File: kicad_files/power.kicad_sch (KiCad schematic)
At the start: 20 parts, among them Q1 FS8205A, U1 BQ27441DRZR-G1A, U2 DW01A, U3 TPS61023DRLR

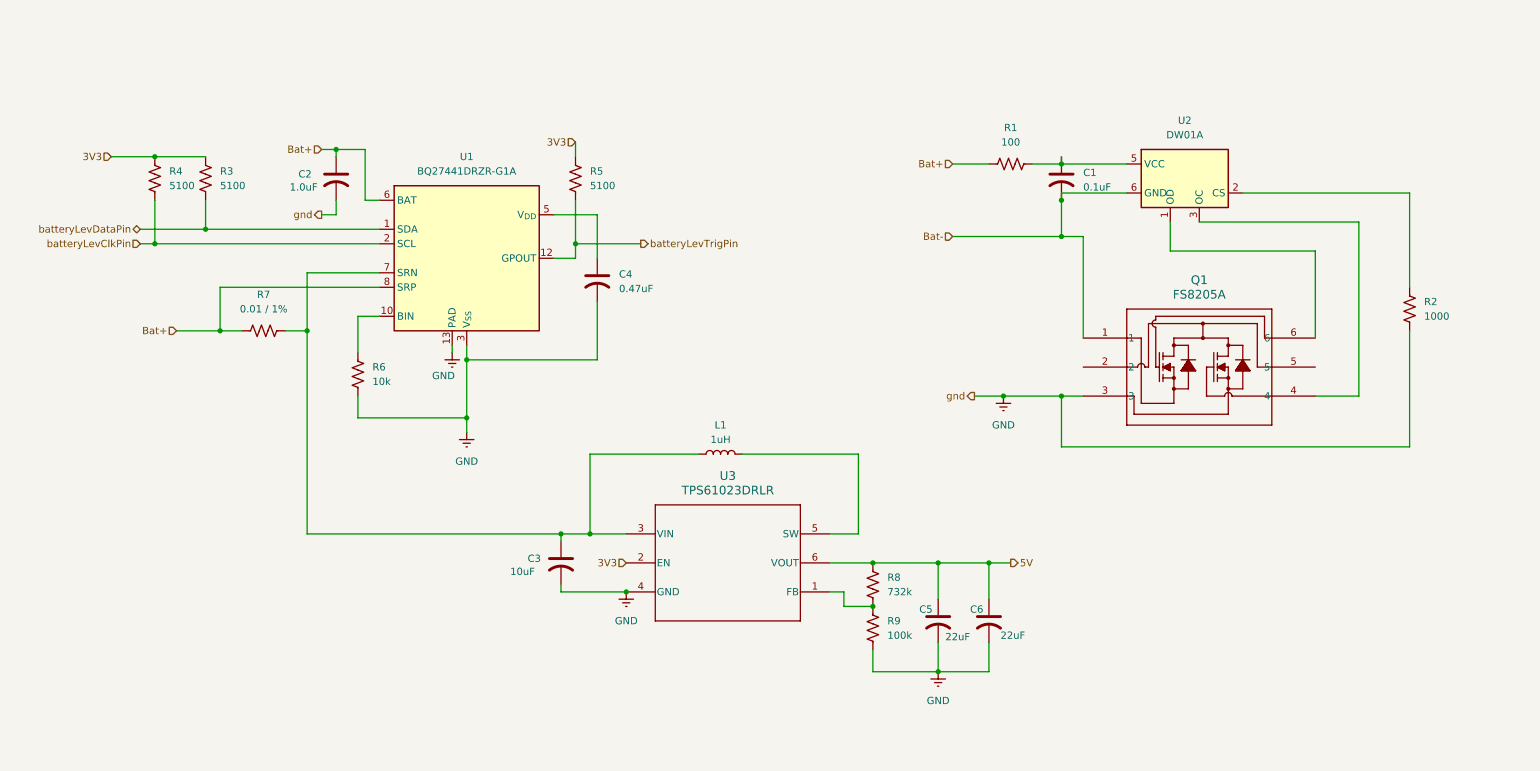
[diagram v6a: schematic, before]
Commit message: ERC errors cleaned. Hierarchical wiring finished. PWM converter change. Motor driver change.
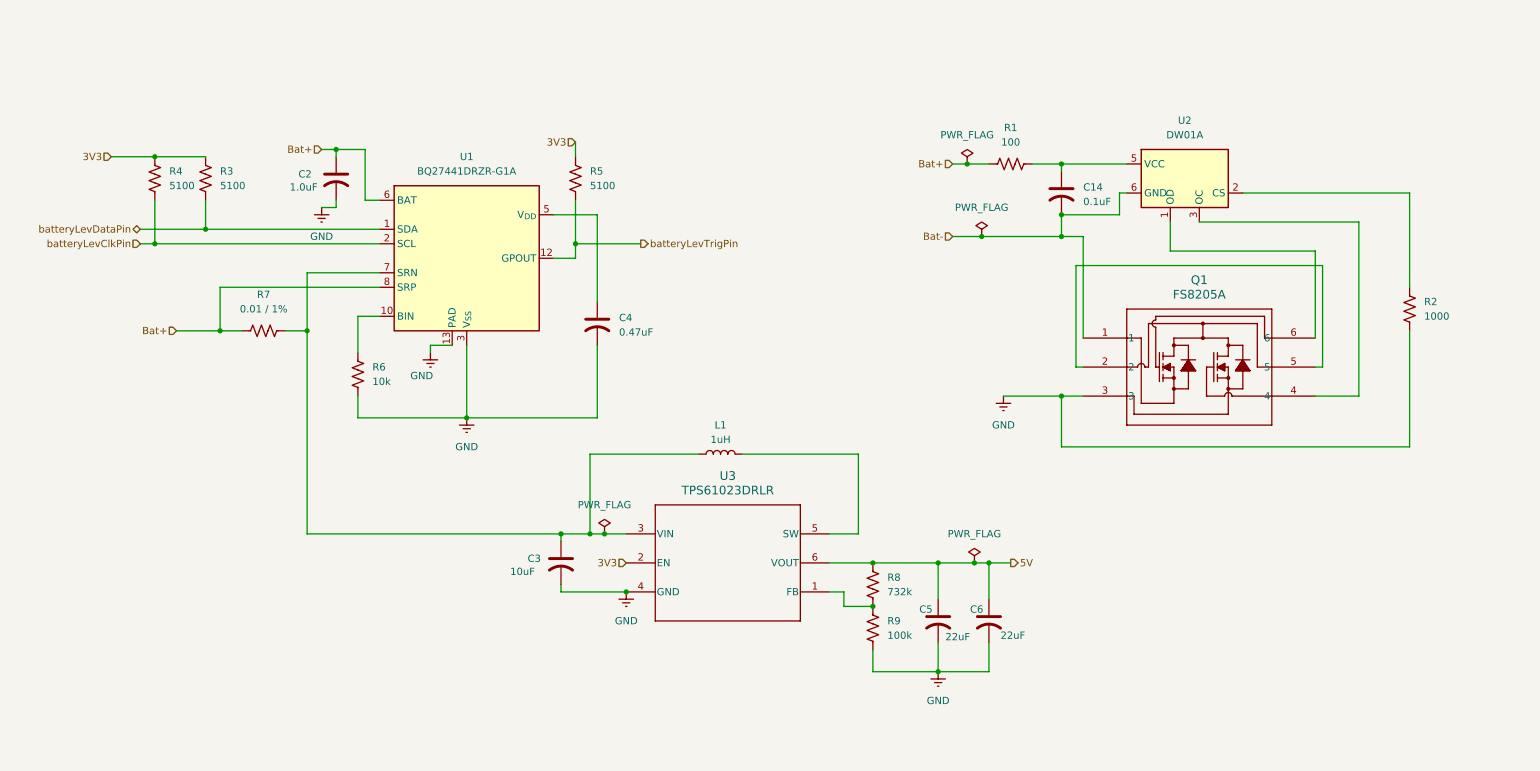
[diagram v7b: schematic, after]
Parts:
- removed C1: 0.1uF, symbol Device:C_US
- added C14: 0.1uF, symbol Device:C_US
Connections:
- net Bat-: now also C14.2
- net at R1.1, U2.5 (VCC): now also C14.1
- net at Q1.2: now also Q1.5
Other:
- moved on the sheet: C4

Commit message: Footprint assignment finished
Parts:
- C14, C2, C3, C4: footprint (none) -> Capacitor_SMD:C_1206_3216Metric_Pad1.33x1.80mm_HandSolder
- C5, C6: footprint (none) -> Capacitor_THT:CP_Radial_D5.0mm_P2.00mm
- L1: footprint (none) -> Inductor_SMD:L_1008_2520Metric_Pad1.43x2.20mm_HandSolder
- R1, R2, R3, R4, R5, R6, R7, R8, R9: footprint (none) -> Resistor_SMD:R_1206_3216Metric_Pad1.30x1.75mm_HandSolder
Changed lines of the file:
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@@
 			)
 		)
-		(property "Footprint" ""
+		(property "Footprint" "Capacitor_SMD:C_1206_3216Metric_Pad1.33x1.80mm_HandSolder"
 			(at 193.04 50.8 0)
 			(effects
@@
 			)
 		)
-		(property "Footprint" ""
+		(property "Footprint" "Resistor_SMD:R_1206_3216Metric_Pad1.30x1.75mm_HandSolder"
 			(at 161.036 119.634 90)
 			(effects
@@
 			)
 		)
-		(property "Footprint" ""
+		(property "Footprint" "Resistor_SMD:R_1206_3216Metric_Pad1.30x1.75mm_HandSolder"
 			(at 183.896 46.736 90)
 			(effects
@@
 			)
 		)
-		(property "Footprint" ""
+		(property "Footprint" "Resistor_SMD:R_1206_3216Metric_Pad1.30x1.75mm_HandSolder"
 			(at 44.196 48.514 90)
 			(effects
@@
 			)
 		)
-		(property "Footprint" ""
+		(property "Footprint" "Resistor_SMD:R_1206_3216Metric_Pad1.30x1.75mm_HandSolder"
 			(at 255.016 71.374 90)
 			(effects
@@
 			)
 		)
-		(property "Footprint" ""
+		(property "Footprint" "Capacitor_SMD:C_1206_3216Metric_Pad1.33x1.80mm_HandSolder"
 			(at 111.76 73.66 0)
 			(effects
@@
 			)
 		)
-		(property "Footprint" ""
+		(property "Footprint" "Capacitor_THT:CP_Radial_D5.0mm_P2.00mm"
 			(at 180.34 125.73 0)
 			(effects
@@
 			)
 		)
-		(property "Footprint" ""
+		(property "Footprint" "Capacitor_SMD:C_1206_3216Metric_Pad1.33x1.80mm_HandSolder"
 			(at 66.04 48.26 0)
 			(effects
@@
 			)
 		)
-		(property "Footprint" ""
+		(property "Footprint" "Inductor_SMD:L_1008_2520Metric_Pad1.43x2.20mm_HandSolder"
 			(at 133.35 96.52 0)
 			(effects
@@
 			)
 		)
-		(property "Footprint" ""
+		(property "Footprint" "Resistor_SMD:R_1206_3216Metric_Pad1.30x1.75mm_HandSolder"
 			(at 53.086 75.946 90)
 			(effects
@@
 			)
 		)
-		(property "Footprint" ""
+		(property "Footprint" "Capacitor_THT:CP_Radial_D5.0mm_P2.00mm"
 			(at 171.45 125.73 0)
 			(effects
@@
 			)
 		)
-		(property "Footprint" ""
+		(property "Footprint" "Capacitor_SMD:C_1206_3216Metric_Pad1.33x1.80mm_HandSolder"
 			(at 105.41 115.57 0)
 			(effects
@@
 			)
 		)
-		(property "Footprint" ""
+		(property "Footprint" "Resistor_SMD:R_1206_3216Metric_Pad1.30x1.75mm_HandSolder"
 			(at 161.036 127.254 90)
 			(effects
@@
 			)
 		)
-		(property "Footprint" ""
+		(property "Footprint" "Resistor_SMD:R_1206_3216Metric_Pad1.30x1.75mm_HandSolder"
 			(at 108.966 48.514 90)
 			(effects
@@
 			)
 		)
-		(property "Footprint" ""
+		(property "Footprint" "Resistor_SMD:R_1206_3216Metric_Pad1.30x1.75mm_HandSolder"
 			(at 35.306 48.514 90)
 			(effects
@@
 			)
 		)
-		(property "Footprint" ""
+		(property "Footprint" "Resistor_SMD:R_1206_3216Metric_Pad1.30x1.75mm_HandSolder"
 			(at 70.866 82.804 90)
 			(effects
